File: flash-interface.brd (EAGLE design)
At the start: 11.2 x 15.2 mm, 3 parts, among them U1 W25N01GVZEIG_TR

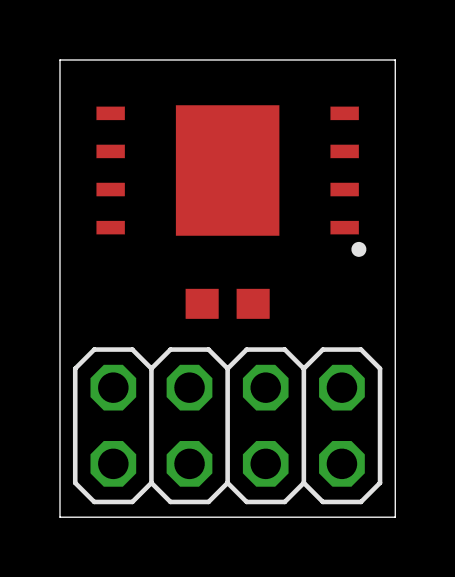
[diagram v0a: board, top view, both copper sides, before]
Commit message: Replaced 0603 cap with 0805, fully routed board
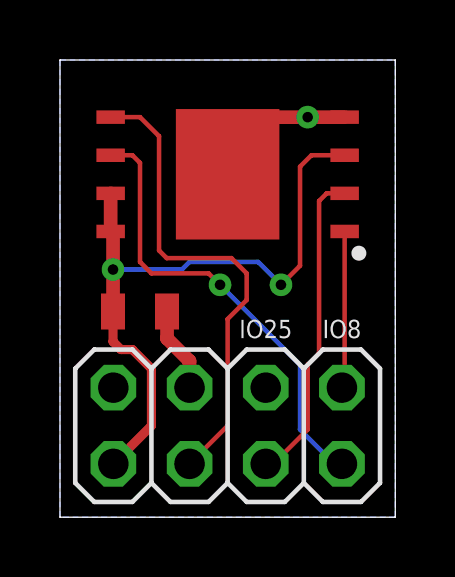
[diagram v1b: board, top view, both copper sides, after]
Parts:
- C1: device SparkFun-Capacitors:0603 -> SparkFun-Capacitors:0805
- moved C1 2.93 mm to (2.67, 6.86)
- moved U1 0.13 mm to (5.59, 11.4)
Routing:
- net VCC: track 0.00 -> 22.2 mm, vias 0 -> 2
- net MOSI: track 0.00 -> 16.1 mm
- net SCLK: track 0.00 -> 15.2 mm, vias 0 -> 1
- net MISO: track 0.00 -> 10.6 mm
- net GND: track 0.00 -> 8.06 mm, vias 0 -> 1
- net !SS: track 0.00 -> 5.24 mm
- added copper zone on layer 16, net GND
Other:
- board text added: "IO25"
- board text added: "IO8"

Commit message: Gave the ground plane more room
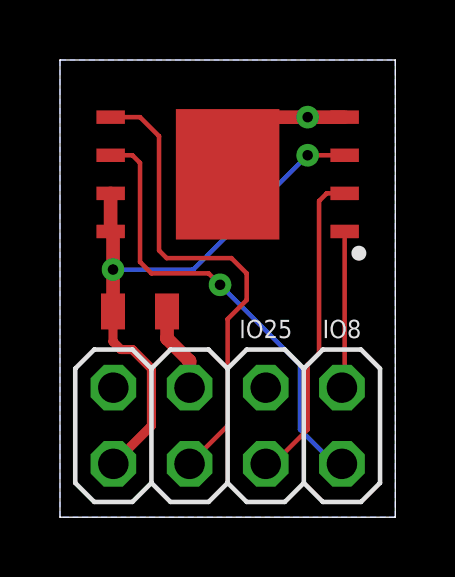
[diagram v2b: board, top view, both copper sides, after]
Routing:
- net VCC: track 22.2 -> 19.6 mm
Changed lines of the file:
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@@
 <via x="1.767" y="8.255" extent="1-16" drill="0.35"/>
 <wire x1="1.767" y1="9.446" x2="1.767" y2="8.255" width="0.4572" layer="1"/>
-<wire x1="9.488" y1="12.065" x2="8.382" y2="12.065" width="0.1524" layer="1"/>
-<wire x1="8.382" y1="12.065" x2="8.001" y2="11.684" width="0.1524" layer="1"/>
-<wire x1="8.001" y1="11.684" x2="8.001" y2="8.382" width="0.1524" layer="1"/>
-<wire x1="8.001" y1="8.382" x2="7.366" y2="7.747" width="0.1524" layer="1"/>
-<via x="7.366" y="7.747" extent="1-16" drill="0.35"/>
-<wire x1="1.767" y1="8.255" x2="4.064" y2="8.255" width="0.1524" layer="16"/>
-<wire x1="6.604" y1="8.509" x2="7.366" y2="7.747" width="0.1524" layer="16"/>
-<wire x1="4.064" y1="8.255" x2="4.318" y2="8.509" width="0.1524" layer="16"/>
-<wire x1="4.318" y1="8.509" x2="6.604" y2="8.509" width="0.1524" layer="16"/>
+<wire x1="9.488" y1="12.065" x2="8.255" y2="12.065" width="0.1524" layer="1"/>
+<via x="8.255" y="12.065" extent="1-16" drill="0.35"/>
+<wire x1="8.255" y1="12.065" x2="4.445" y2="8.255" width="0.1524" layer="16"/>
+<wire x1="4.445" y1="8.255" x2="1.767" y2="8.255" width="0.1524" layer="16"/>
 </signal>
 <signal name="!SS">
